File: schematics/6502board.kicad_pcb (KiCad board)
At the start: 2 copper layers, 35 x 103 mm, 35 parts, among them J1 Power, J2 DEBUG, J3 I2C, J4 Serial, J5 Spare CS, SW1 Reset, U1 W65C02S6TQG, U10 TL16C750E, U2 IS61LV256AL, U3 74LVC139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

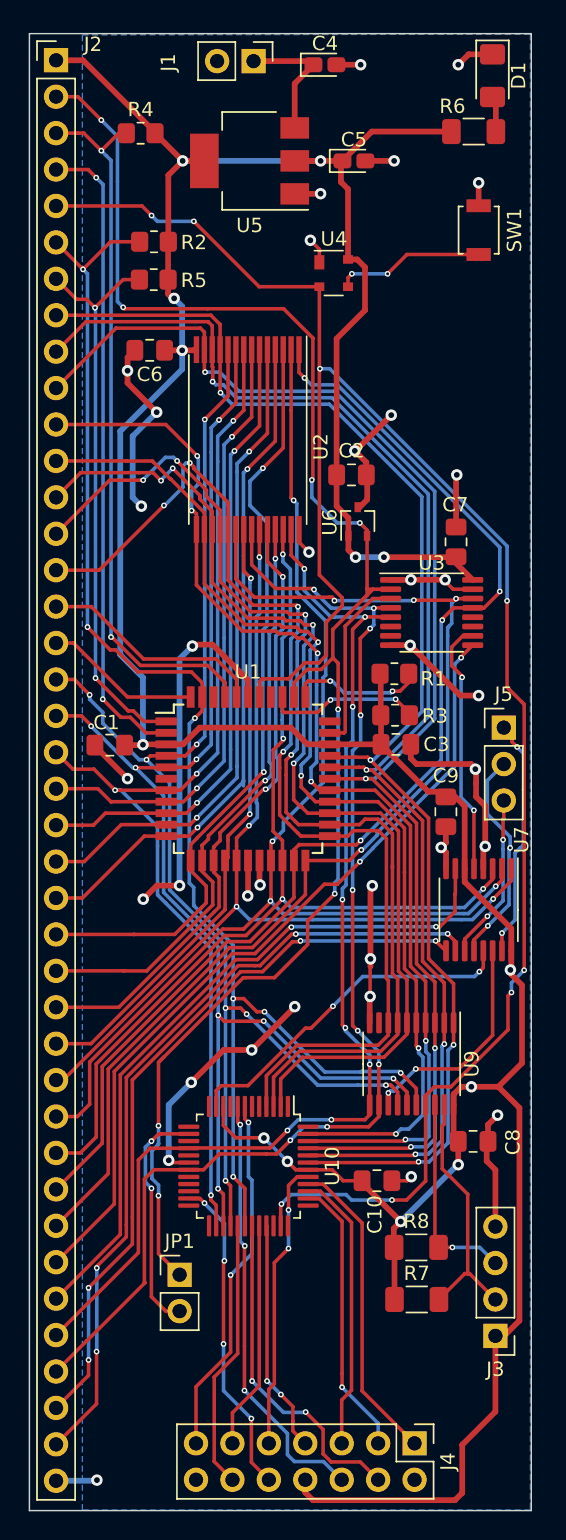
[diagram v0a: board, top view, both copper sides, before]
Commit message: Invert IRQ and RESET for UART. Experiment with vias.
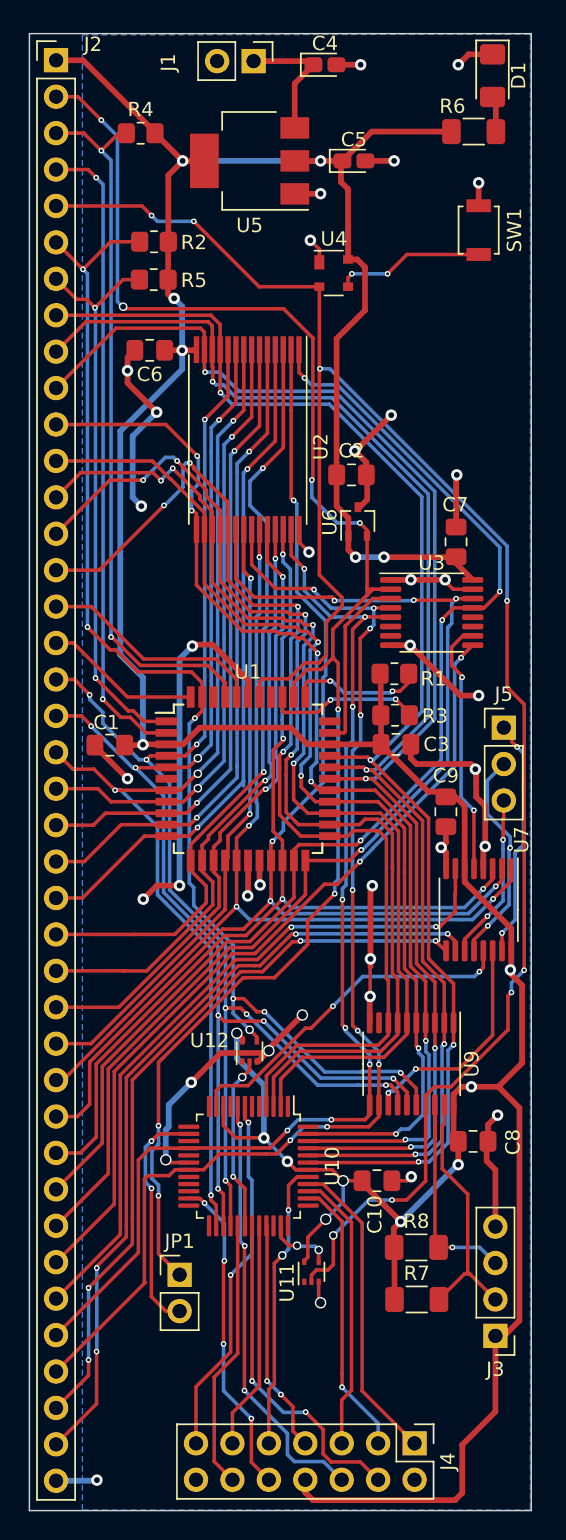
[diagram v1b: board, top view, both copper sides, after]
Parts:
- added U11: 74LVC1GU04DRL, Package_TO_SOT_SMD:SOT-553, F.Cu at (34.7, 101.3)
- added U12: 74LVC1GU04DRL, Package_TO_SOT_SMD:SOT-553, F.Cu at (30.4, 86.0)
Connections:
- net Net-(J4-Pad10) renamed UART_TXRDY
- net Net-(J4-Pad11) renamed UART_RTS
- net Net-(J4-Pad12) renamed UART_RXRDY
- net Net-(J4-Pad13) renamed UART_RX
- net Net-(J4-Pad3) renamed UART_CTS
- net Net-(J4-Pad4) renamed UART_OP
- net Net-(J4-Pad5) renamed UART_DSR
- net Net-(J4-Pad6) renamed UART_TX
- net Net-(J4-Pad7) renamed UART_DTR
- net Net-(J4-Pad9) renamed UART_RI
- net Net-(U10-Pad40) renamed UART_CD
- U10 pad 30: _IRQ -> Net-(U12-Pad2)
- U10 pad 35: _RESET -> Net-(U10-Pad35)
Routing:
- net VCC: track 252.7 -> 268.3 mm, vias 13 -> 16
- net _IRQ: track 98.5 -> 86.0 mm
- net Net-(U12-Pad2): track 0.00 -> 12.3 mm, vias 0 -> 2
- net Net-(U10-Pad35): track 0.00 -> 4.65 mm, vias 0 -> 2
- net GND: track 141.3 -> 144.8 mm, vias 36 -> 37
